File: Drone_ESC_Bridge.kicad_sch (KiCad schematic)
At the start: 21 parts, among them Q1 Si2318CDS, U1 LMP8640, U2 LM5050-1

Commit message: Initial board revision
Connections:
- net VSENSE: now also XIAO_L1.7 (Pin_7); no longer XIAO_L1.6 (Pin_6)
- net at ESC1.6 (Pin_6), ESC_DEBUG1.1 (Pin_1): now also XIAO_L1.4 (Pin_4); no longer XIAO_L1.3 (Pin_3)
- net at ESC1.5 (Pin_5), ESC_DEBUG1.2 (Pin_2): now also XIAO_L1.5 (Pin_5); no longer XIAO_L1.4 (Pin_4)
- net at ESC1.7 (Pin_7), ESC_DEBUG1.4 (Pin_4): now also XIAO_L1.3 (Pin_3); no longer XIAO_L1.2 (Pin_2)
- net at XIAO_R1.4 (Pin_4): now also SPI1.4 (Pin_4); no longer SPI1.2 (Pin_2)
- net at XIAO_R1.6 (Pin_6): now also SPI1.2 (Pin_2); no longer SPI1.3 (Pin_3)
- net at ESC1.4 (Pin_4): now also XIAO_L1.6 (Pin_6); no longer XIAO_L1.5 (Pin_5)
- new net: SPI1.3 (Pin_3), XIAO_L1.2 (Pin_2)
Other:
- note added: "5V GND 3V3 D10/CS D9/SCK D8/MOSI D7/ESC_TELEMETRY"
- note added: "D0/M4 D1/MISO D2/M3 D3/M2 D4/M1 D5/ESC_CURRENT D6/PERIPHERAL_CURRENT"
- note added: "SCK MOSI MISO CS"
- note removed: "5V GND 3V3 D10/MOSI D9/MISO D8/SCK D7/ESC_TELEMETRY"
- note removed: "D0/M4 D1/M3 D2/M2 D3/M1 D4/ESC_CURRENT D5/PERIPHERAL_CURRENT D6/CS"
- note removed: "MISO MOSI SCK CS"
- title: (none) -> Drone ESC Bridge
- moved on the sheet: ESC1, XIAO_L1

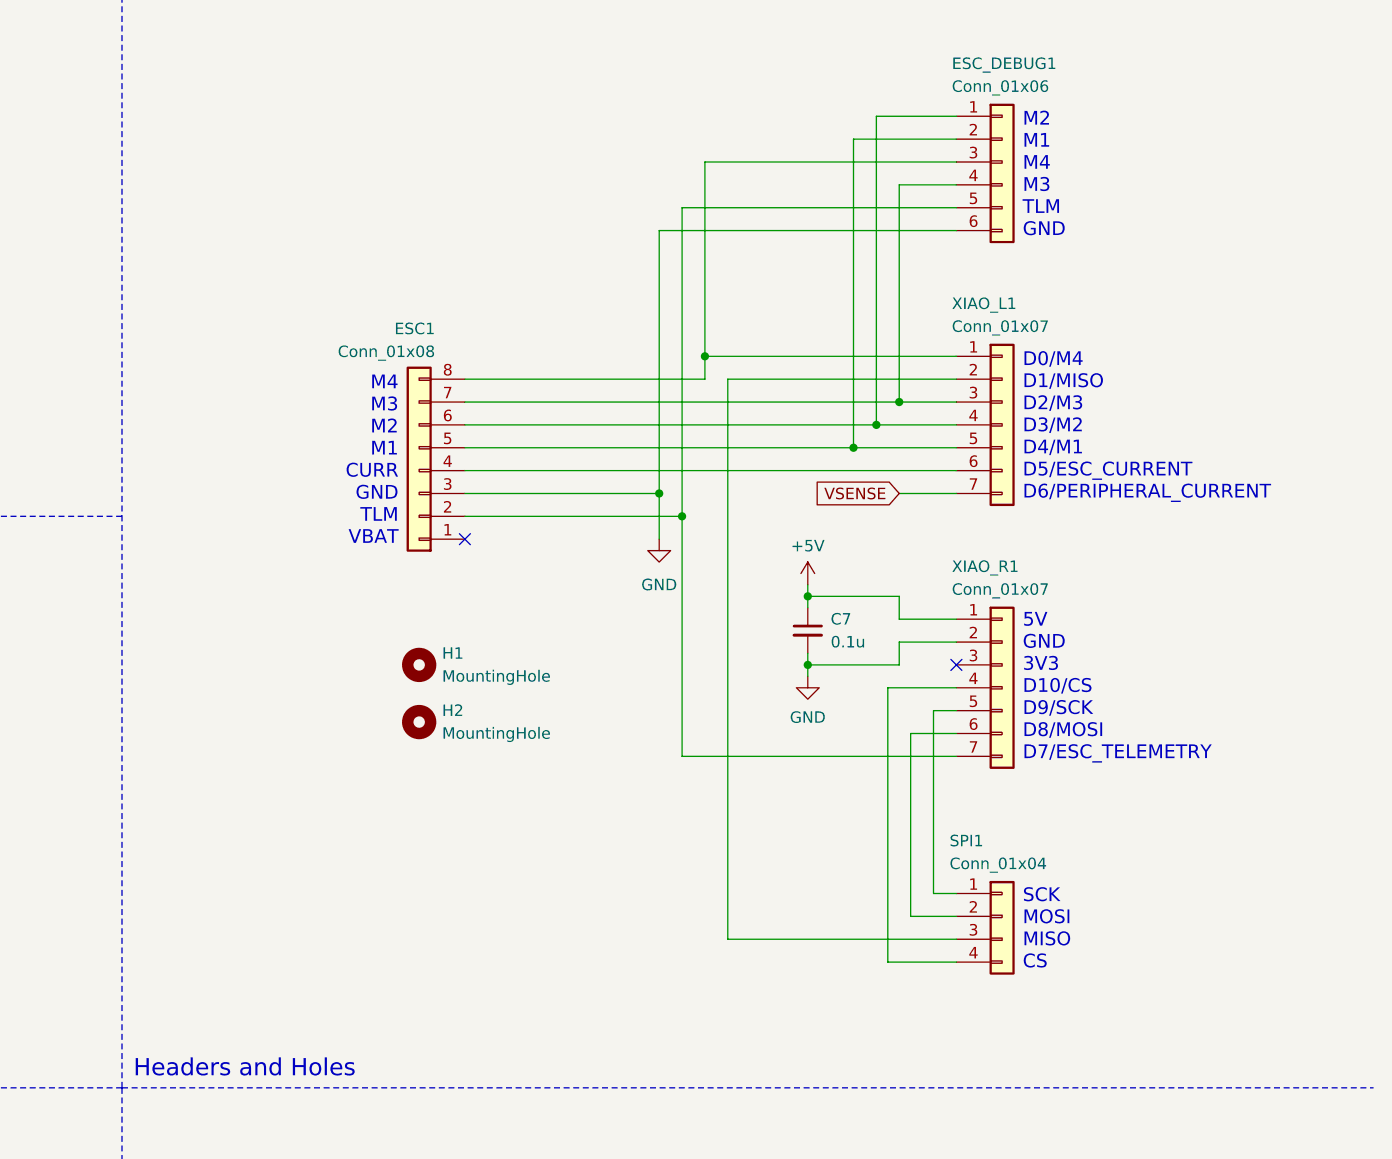
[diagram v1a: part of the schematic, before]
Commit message: Replace telemetry with VBat sense
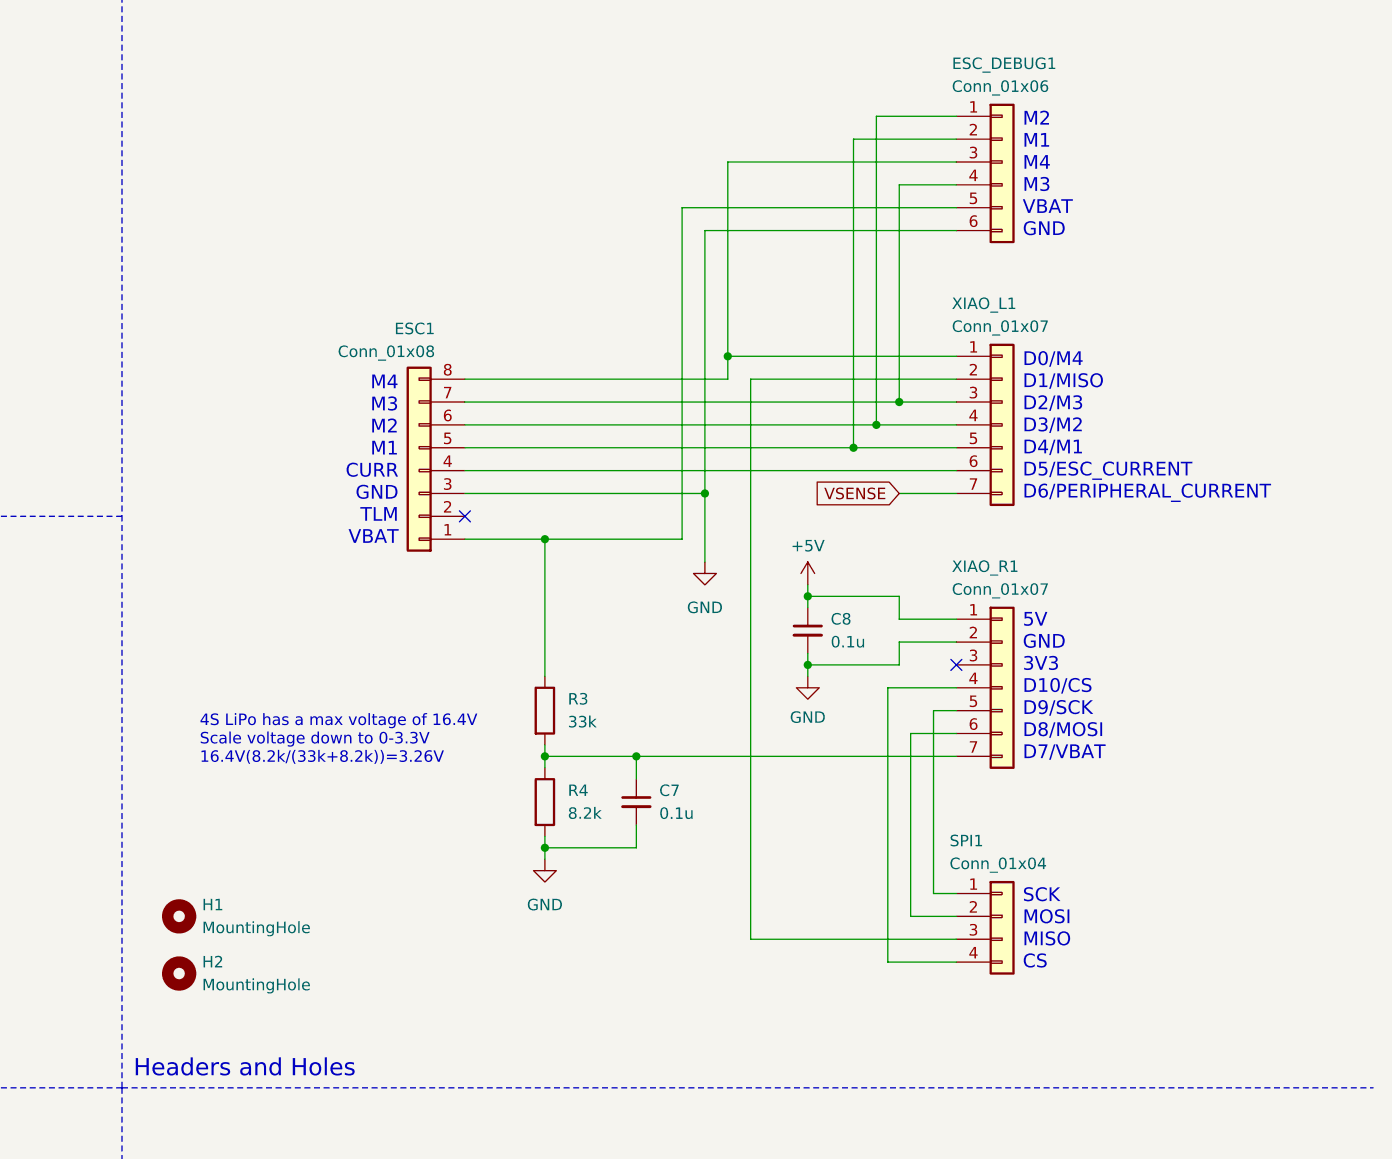
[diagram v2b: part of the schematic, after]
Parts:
- added C7: 0.1u, Capacitor_SMD:C_0603_1608Metric_Pad1.08x0.95mm_HandSolder, symbol Device:C_Small
- added R3: 33k, Resistor_SMD:R_0603_1608Metric_Pad0.98x0.95mm_HandSolder, symbol Device:R
- added R4: 8.2k, Resistor_SMD:R_0603_1608Metric_Pad0.98x0.95mm_HandSolder, symbol Device:R
- renumbered C7 to C8
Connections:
- net GND: now also C7.2, R4.2
- net at ESC1.1 (Pin_1): now also ESC_DEBUG1.5 (Pin_5), R3.1
- new net: C7.1, R3.2, R4.1, XIAO_R1.7 (Pin_7)
- now unconnected: ESC1.2 (Pin_2)
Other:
- note added: "4S LiPo has a max voltage of 16.4V Scale voltage down to 0-3.3V 16.4V(8.2k/(33k+8.2k))=3.26V"
- note added: "5V GND 3V3 D10/CS D9/SCK D8/MOSI D7/VBAT"
- note added: "M2 M1 M4 M3 VBAT GND"
- note removed: "5V GND 3V3 D10/CS D9/SCK D8/MOSI D7/ESC_TELEMETRY"
- note removed: "M2 M1 M4 M3 TLM GND"
- moved on the sheet: H1, H2

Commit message: Add BOM and update ibom
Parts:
- R3: Part Number (none) -> 311-33.0KHRTR-ND
- R4: Part Number (none) -> 311-8.2KGRTR-ND
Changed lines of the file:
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@@
+			)
+		)
+		(property "Part Number" "311-8.2KGRTR-ND"
+			(at 193.04 107.95 0)
+			(effects
+				(font
+					(size 1.27 1.27)
+				)
+				(hide yes)
 			)
 		)
@@
 			(at 193.04 97.79 0)
 			(effects
+				(font
+					(size 1.27 1.27)
+				)
+				(hide yes)
+			)
+		)
+		(property "Part Number" "311-33.0KHRTR-ND"
+			(at 193.04 97.79 0)
+			(effects
